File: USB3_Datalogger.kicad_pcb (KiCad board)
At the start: 6 copper layers, 68.5 x 55 mm, 132 parts, among them J101 Conn_02x20_Odd_Even, J102 Conn_02x07_Odd_Even, J103 Conn_02x07_Odd_Even, J201 USB3-micro, J801 USB_B_Mini, J802 Conn_01x06, SW101 SW_Push, U101 ASDMB-xxxMHz, U201 FT600, U202 TPD2EUSB30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

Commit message: Added SWD header to flash and debug STM32 chip
Signed-off-by: Alexis Jeandet <alexis.jeandet@member.fsf.org>
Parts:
- added J601: Conn_01x05, Connector_PinHeader_2.54mm:PinHeader_1x05_P2.54mm_Vertical, F.Cu at (101.0, 193.0)
- C803: moved to B.Cu
- moved R608 4.13 mm to (89.4, 184.9)
- moved LOGO101 3.66 mm to (94.0, 187.8)
- moved C803 1.87 mm to (103.4, 193.9)
- moved DONE401 0.76 mm to (97.8, 184.2)
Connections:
- U801 pad 2: (no net) -> /FPGA/FLASH_CDONE
- U801 pad 3: (no net) -> /FPGA/FLASH_~CRESET
- U801 pad 46: /FPGA/FLASH_CDONE -> /STM32/SWDIO
- U801 pad 49: /FPGA/FLASH_~CRESET -> /STM32/SWCLK
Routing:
- net /STM32/RESET: track 8.26 -> 33.9 mm, vias 0 -> 1
- net /STM32/SWCLK: track 0.00 -> 14.9 mm, vias 0 -> 1
- net /STM32/SWDIO: track 0.00 -> 11.9 mm, vias 0 -> 1
- net /FPGA/FLASH_~CRESET: track 40.4 -> 34.4 mm
- net VCCIO_0: track 101.7 -> 103.5 mm
- net /FPGA/FLASH_CDONE: track 49.2 -> 48.4 mm
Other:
- board text added: "3.3V"
- board text added: "CLK"
- board text added: "DIO"
- board text added: "RST"
- board text added: "RXD"
- board text added: "TXD"

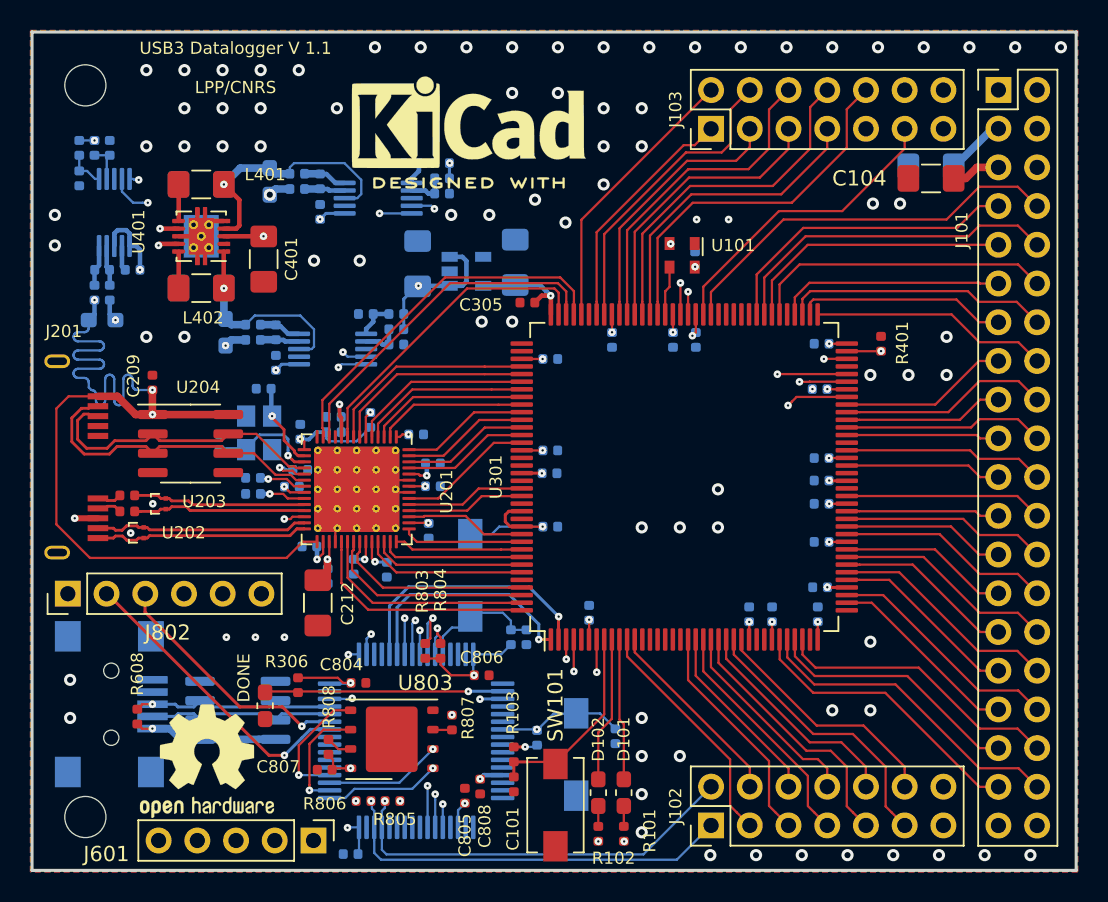
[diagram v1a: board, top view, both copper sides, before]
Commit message: Moved FPGA signals to inner layers, many other fixes
Signed-off-by: Alexis Jeandet <alexis.jeandet@member.fsf.org>
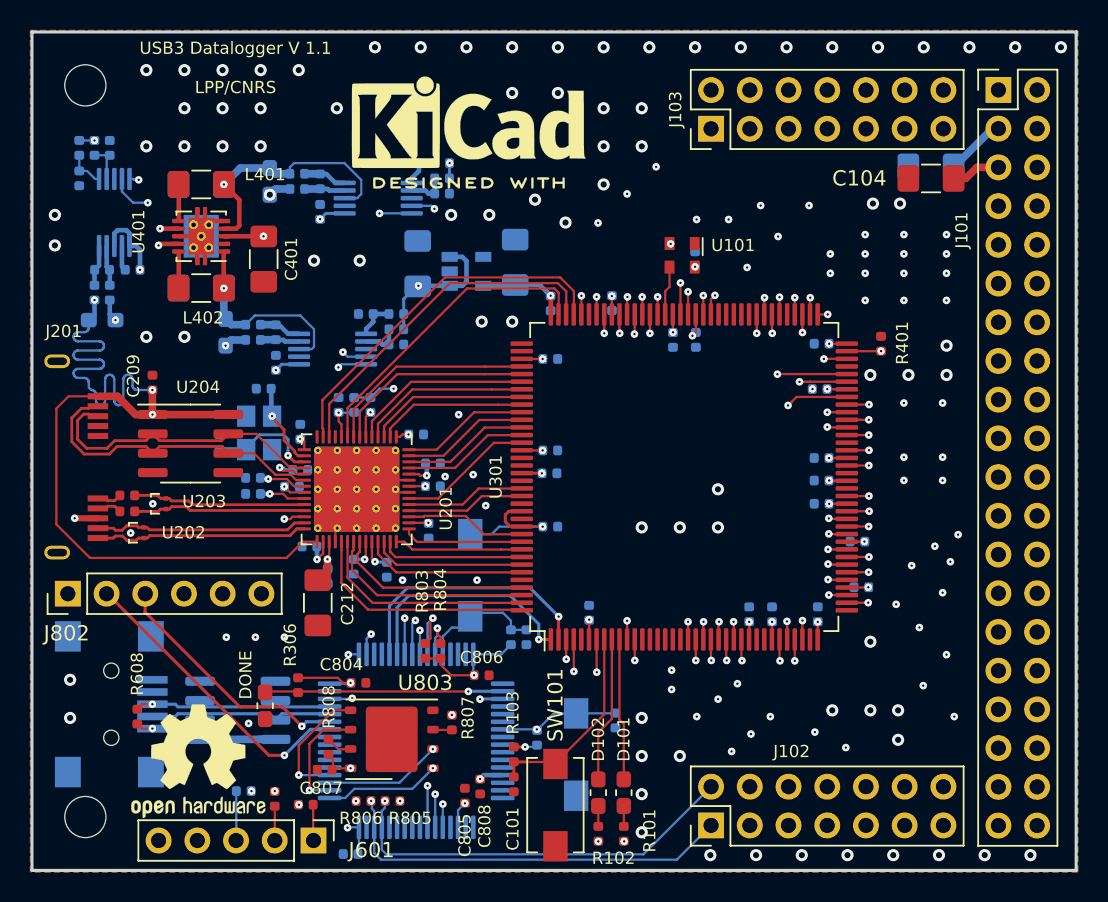
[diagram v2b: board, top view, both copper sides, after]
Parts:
- added R609: 22, Resistor_SMD:R_0402_1005Metric, F.Cu at (100.5, 190.7)
- added R610: 22, Resistor_SMD:R_0402_1005Metric, F.Cu at (98.4, 190.3)
- added R611: 22, Resistor_SMD:R_0402_1005Metric, B.Cu at (96.4, 189.8)
- C305: moved to B.Cu
- moved C318 2.71 mm to (136.9, 176.4)
- moved C302 2.42 mm to (120.5, 157.8)
- moved C312 2.35 mm to (136.7, 173.4)
- moved R202 2.23 mm to (103.6, 164.5), turned to 270 degrees
- moved C305 1.52 mm to (116.5, 157.8), turned to 270 degrees
- moved C802 1.03 mm to (120.8, 185.2)
- moved R203 0.99 mm to (104.7, 164.5), turned to 270 degrees
- moved C217 0.85 mm to (102.6, 164.5), turned to 90 degrees
- moved LOGO101 0.57 mm to (93.4, 187.8)
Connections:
- J601 pad 1: /STM32/SWDIO -> Net-(J601-Pad1)
- J601 pad 2: /STM32/SWCLK -> Net-(J601-Pad2)
- J601 pad 3: /STM32/RESET -> Net-(J601-Pad3)
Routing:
- net VCCIO_0: track 103.5 -> 92.3 mm, vias 31 -> 32
- net /STM32/RESET: track 33.9 -> 28.3 mm, vias 1 -> 2
- net Net-(J601-Pad3): track 0.00 -> 4.42 mm
- net /STM32/SWCLK: track 14.9 -> 11.7 mm, vias 1 -> 2
- net /IOL_21: track 21.1 -> 23.9 mm, vias 0 -> 1
- net /IOB_5: track 11.8 -> 14.3 mm, vias 0 -> 1
- net /IOB_3: track 12.4 -> 14.9 mm, vias 0 -> 1
- net /IOB_7: track 11.1 -> 13.6 mm, vias 0 -> 1
- net /IOL_8: track 15.5 -> 18.0 mm, vias 0 -> 1
- net /IOB_16: track 13.2 -> 15.7 mm, vias 0 -> 1
- net /IOB_10: track 13.5 -> 15.8 mm, vias 0 -> 1
- net /IOB_8: track 14.1 -> 16.5 mm, vias 0 -> 1
- net /IOB_2: track 15.6 -> 18.0 mm, vias 0 -> 1
- net Net-(J601-Pad1): track 0.00 -> 2.36 mm
- net /IOL_10: track 14.9 -> 17.3 mm, vias 0 -> 1
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- added copper zone on In2.Cu, net /USB3/VD10
- removed copper zone on In3.Cu, net /USB3/VD10
- removed copper zone on In2.Cu, net VCCIO_0
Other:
- board text added: "GND"
